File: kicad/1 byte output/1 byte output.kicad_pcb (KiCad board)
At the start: 2 copper layers, 52.1 x 53.3 mm, 9 parts, among them J1 Conn_01x05_Male, J2 Conn_01x05_Female, J3 Conn_01x08, J4 Screw_Terminal_01x02, U1 74HCT595, U2 ULN2803A

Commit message: periodic check in
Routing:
- net GND: track 0.00 -> 124.3 mm, vias 0 -> 1
- net VCC: track 19.2 -> 75.0 mm, vias 0 -> 2
- net DO: track 0.00 -> 21.6 mm, vias 0 -> 1
- net LAT: track 41.8 -> 58.4 mm, vias 0 -> 1
- net CLK: track 41.8 -> 55.9 mm, vias 0 -> 1
- net COM: track 0.00 -> 12.7 mm
- net OUT1: track 12.6 -> 17.8 mm
- net OUT2: track 11.5 -> 15.2 mm
- net OUT7: track 11.5 -> 15.2 mm
- net Net-(U1-Pad15): track 12.6 -> 9.52 mm
- net OUT8: track 14.8 -> 17.8 mm
- net OUT3: track 10.5 -> 12.7 mm
- net OUT6: track 10.5 -> 12.7 mm
- net DI: track 30.9 -> 32.4 mm, vias 0 -> 1
- net OUT5: track 9.42 -> 10.2 mm
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- removed copper zone on B.Cu, net GND
- removed copper zone on F.Cu, net VCC

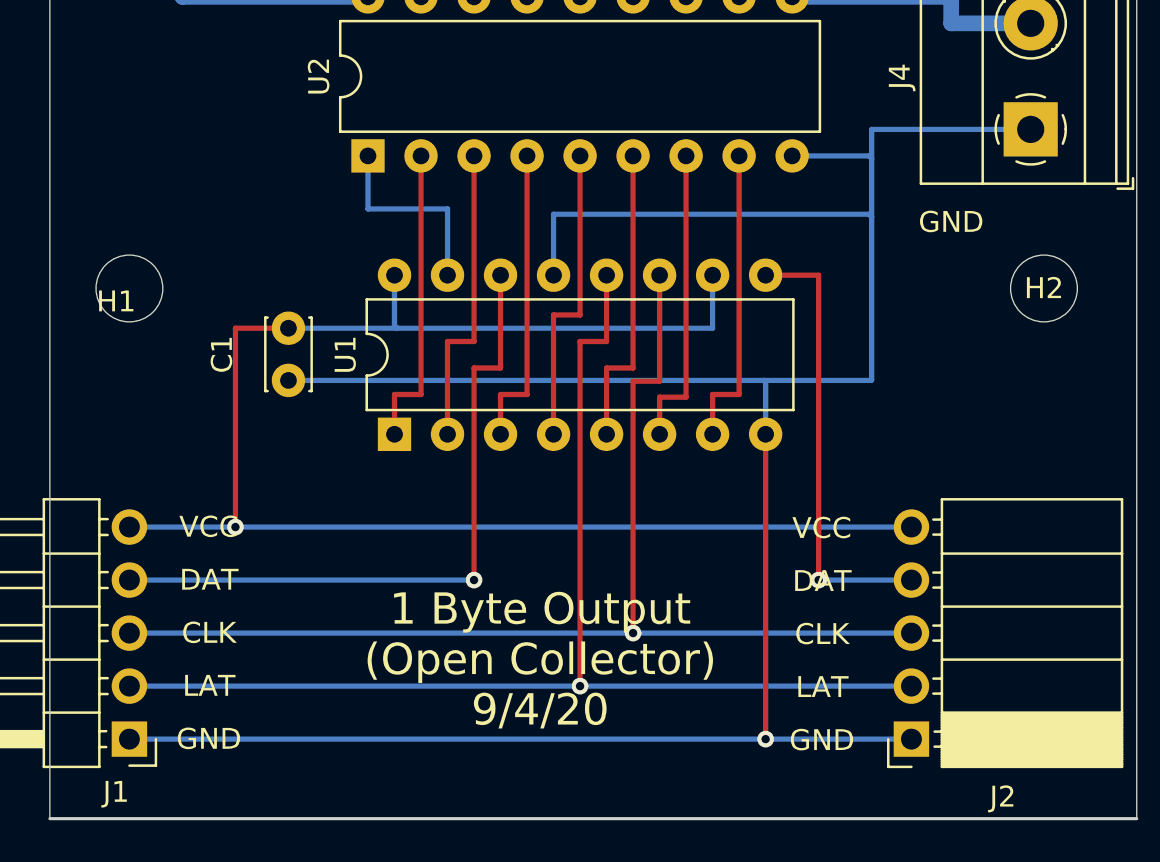
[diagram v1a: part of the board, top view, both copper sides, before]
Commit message: rerouted several PCBs
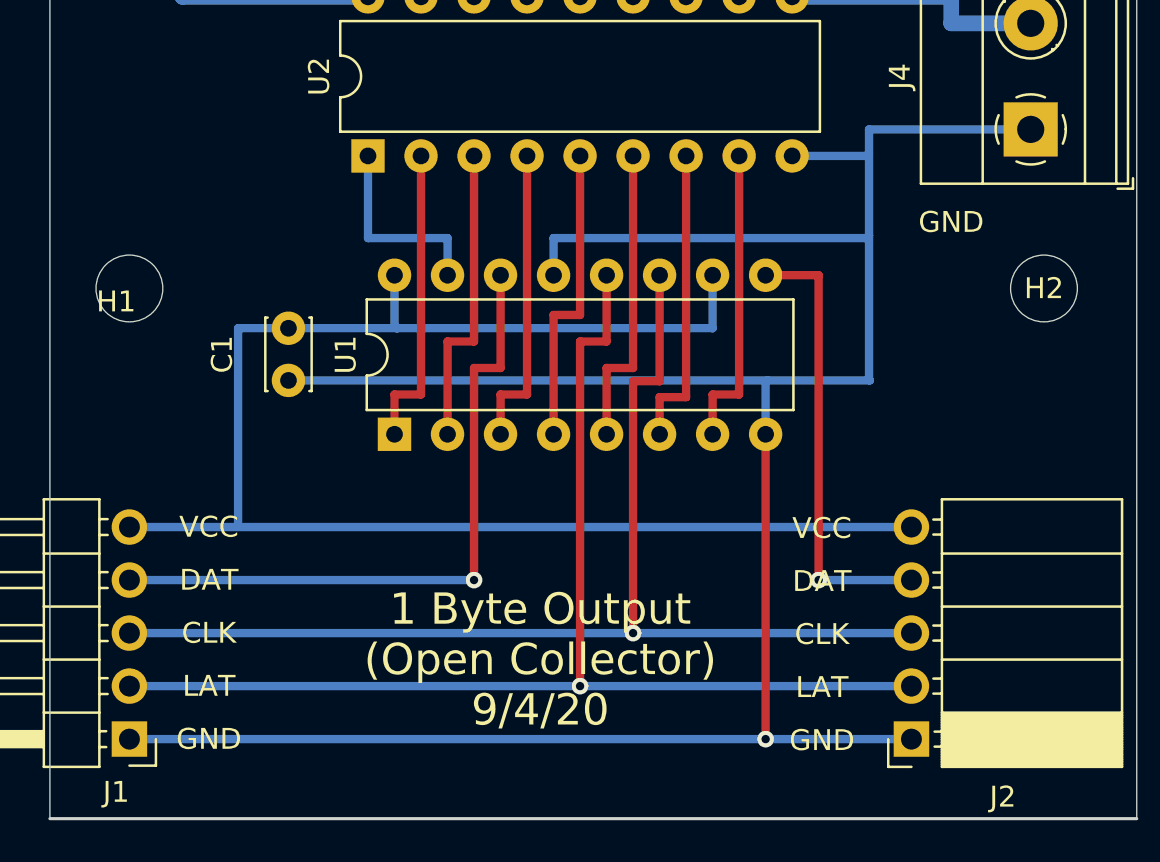
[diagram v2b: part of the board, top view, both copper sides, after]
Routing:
- net GND: track 124.3 -> 123.0 mm
- net VCC: track 75.0 -> 74.9 mm, vias 2 -> 1

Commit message: added dcc sniffer, conversion to kicad 6
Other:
- net class Default removed
- net class power removed
